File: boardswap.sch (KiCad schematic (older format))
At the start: 154 parts, among them J1 USB_C_Receptacle_USB2.0, SW1 SW_Push, U1 ATmega32U4-AU, Y1 16MHz

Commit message: did most placement
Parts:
- C7: footprint Diode_SMD:D_SOD-123 -> Capacitor_SMD:C_0805_2012Metric
- J1: footprint keyswitches:Kailh_socket_MX -> Connector_USB:USB_C_Receptacle_HRO_TYPE-C-31-M-12
- U1: footprint Package_QFP:TQFP-44_10x10mm_P0.8mm -> Package_DFN_QFN:QFN-44-1EP_7x7mm_P0.5mm_EP5.2x5.2mm
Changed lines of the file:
@@
 F 0 "J1" H 1307 7367 50  0000 C CNN
 F 1 "USB_C_Receptacle_USB2.0" H 1307 7276 50  0000 C CNN
-F 2 "keyswitches:Kailh_socket_MX" H 1350 6500 50  0001 C CNN
+F 2 "Connector_USB:USB_C_Receptacle_HRO_TYPE-C-31-M-12" H 1350 6500 50  0001 C CNN
 F 3 "https://www.usb.org/sites/default/files/documents/usb_type-c.zip" H 1350 6500 50  0001 C CNN
 	1    1200 6500
@@
 F 0 "C7" H 2042 3746 50  0000 L CNN
 F 1 "10uF" H 2042 3655 50  0000 L CNN
-F 2 "Diode_SMD:D_SOD-123" H 1950 3700 50  0001 C CNN
+F 2 "Capacitor_SMD:C_0805_2012Metric" H 1950 3700 50  0001 C CNN
 F 3 "~" H 1950 3700 50  0001 C CNN
 	1    1950 3700
@@
 F 0 "U1" H 3400 1111 50  0000 C CNN
 F 1 "ATmega32U4-AU" H 3400 1020 50  0000 C CNN
-F 2 "Package_QFP:TQFP-44_10x10mm_P0.8mm" H 3400 3000 50  0001 C CIN
+F 2 "Package_DFN_QFN:QFN-44-1EP_7x7mm_P0.5mm_EP5.2x5.2mm" H 3400 3000 50  0001 C CIN
 F 3 "http://ww1.microchip.com/downloads/en/DeviceDoc/Atmel-7766-8-bit-AVR-ATmega16U4-32U4_Datasheet.pdf" H 3400 3000 50  0001 C CNN
 	1    3400 3000

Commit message: hewwo backups owo
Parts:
- U1: footprint Package_DFN_QFN:QFN-44-1EP_7x7mm_P0.5mm_EP5.2x5.2mm -> Package_QFP:TQFP-44_10x10mm_P0.8mm
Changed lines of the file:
@@
 F 0 "U1" H 3400 1111 50  0000 C CNN
 F 1 "ATmega32U4-AU" H 3400 1020 50  0000 C CNN
-F 2 "Package_DFN_QFN:QFN-44-1EP_7x7mm_P0.5mm_EP5.2x5.2mm" H 3400 3000 50  0001 C CIN
+F 2 "Package_QFP:TQFP-44_10x10mm_P0.8mm" H 3400 3000 50  0001 C CIN
 F 3 "http://ww1.microchip.com/downloads/en/DeviceDoc/Atmel-7766-8-bit-AVR-ATmega16U4-32U4_Datasheet.pdf" H 3400 3000 50  0001 C CNN
 	1    3400 3000

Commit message: placed components
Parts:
- C4, C5, C6, C7: footprint Capacitor_SMD:C_0805_2012Metric -> Capacitor_SMD:C_0603_1608Metric
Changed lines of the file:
@@
 	1    0    0    -1
 $EndComp
-Connection ~ 2800 1500
 Wire Wire Line
 	2300 1500 2300 1200
@@
 	1    0    0    -1
 $EndComp
-Wire Wire Line
-	2800 1500 2800 1250
 $Comp
 L Device:R_Small R1
@@
 F 0 "C7" H 2042 3746 50  0000 L CNN
 F 1 "10uF" H 2042 3655 50  0000 L CNN
-F 2 "Capacitor_SMD:C_0805_2012Metric" H 1950 3700 50  0001 C CNN
+F 2 "Capacitor_SMD:C_0603_1608Metric" H 1950 3700 50  0001 C CNN
 F 3 "~" H 1950 3700 50  0001 C CNN
 	1    1950 3700
@@
 F 0 "C6" H 1642 3746 50  0000 L CNN
 F 1 "0.1uF" H 1642 3655 50  0000 L CNN
-F 2 "Capacitor_SMD:C_0805_2012Metric" H 1550 3700 50  0001 C CNN
+F 2 "Capacitor_SMD:C_0603_1608Metric" H 1550 3700 50  0001 C CNN
 F 3 "~" H 1550 3700 50  0001 C CNN
 	1    1550 3700
@@
 F 0 "C5" H 1242 3746 50  0000 L CNN
 F 1 "0.1uF" H 1242 3655 50  0000 L CNN
-F 2 "Capacitor_SMD:C_0805_2012Metric" H 1150 3700 50  0001 C CNN
+F 2 "Capacitor_SMD:C_0603_1608Metric" H 1150 3700 50  0001 C CNN
 F 3 "~" H 1150 3700 50  0001 C CNN
 	1    1150 3700
@@
 F 0 "C4" H 842 3746 50  0000 L CNN
 F 1 "0.1uF" H 842 3655 50  0000 L CNN
-F 2 "Capacitor_SMD:C_0805_2012Metric" H 750 3700 50  0001 C CNN
+F 2 "Capacitor_SMD:C_0603_1608Metric" H 750 3700 50  0001 C CNN
 F 3 "~" H 750 3700 50  0001 C CNN
 	1    750  3700
@@
 $EndComp
 Wire Wire Line
-	3300 4800 2950 4800
-Connection ~ 3300 4800
-Wire Wire Line
-	2950 4800 2950 4900
-Wire Wire Line
-	3400 4800 3300 4800
-$Comp
-L power:GND #PWR0109
-U 1 1 5F31D09C
-P 2950 4900
-F 0 "#PWR0109" H 2950 4650 50  0001 C CNN
-F 1 "GND" H 2955 4727 50  0000 C CNN
-F 2 "" H 2950 4900 50  0001 C CNN
-F 3 "" H 2950 4900 50  0001 C CNN
-	1    2950 4900
-	1    0    0    -1
-$EndComp
-Wire Wire Line
-	3400 1200 3400 1050
-Wire Wire Line
 	3400 1200 3500 1200
 Connection ~ 3400 1200
@@
 F 3 "" H 3400 1050 50  0001 C CNN
 	1    3400 1050
-	1    0    0    -1
-$EndComp
-$Comp
-L MCU_Microchip_ATmega:ATmega32U4-AU U1
-U 1 1 5F319131
-P 3400 3000
-F 0 "U1" H 3400 1111 50  0000 C CNN
-F 1 "ATmega32U4-AU" H 3400 1020 50  0000 C CNN
-F 2 "Package_QFP:TQFP-44_10x10mm_P0.8mm" H 3400 3000 50  0001 C CIN
-F 3 "http://ww1.microchip.com/downloads/en/DeviceDoc/Atmel-7766-8-bit-AVR-ATmega16U4-32U4_Datasheet.pdf" H 3400 3000 50  0001 C CNN
-	1    3400 3000
 	1    0    0    -1
 $EndComp
@@
 Text GLabel 10500 1200 1    50   Input ~ 0
 COL13
+Wire Wire Line
+	3400 1200 3400 1050
+Wire Wire Line
+	2800 1500 2800 1250
+$Comp
+L power:GND #PWR0109
+U 1 1 5F31D09C
+P 2950 4900
+F 0 "#PWR0109" H 2950 4650 50  0001 C CNN
+F 1 "GND" H 2955 4727 50  0000 C CNN
+F 2 "" H 2950 4900 50  0001 C CNN
+F 3 "" H 2950 4900 50  0001 C CNN
+	1    2950 4900
+	1    0    0    -1
+$EndComp
+Connection ~ 2800 1500
+Wire Wire Line
+	2950 4800 2950 4900
+$Comp
+L MCU_Microchip_ATmega:ATmega32U4-AU U1
+U 1 1 5F319131
+P 3400 3000
+F 0 "U1" H 3400 1111 50  0000 C CNN
+F 1 "ATmega32U4-AU" H 3400 1020 50  0000 C CNN
+F 2 "Package_QFP:TQFP-44_10x10mm_P0.8mm" H 3400 3000 50  0001 C CIN
+F 3 "http://ww1.microchip.com/downloads/en/DeviceDoc/Atmel-7766-8-bit-AVR-ATmega16U4-32U4_Datasheet.pdf" H 3400 3000 50  0001 C CNN
+	1    3400 3000
+	1    0    0    -1
+$EndComp
+Wire Wire Line
+	3400 4800 3300 4800
+Connection ~ 3300 4800
+Wire Wire Line
+	2950 4800 3300 4800
 $EndSCHEMATC

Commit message: done routing probably
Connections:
- net COL0: now also U1.11 (PB3)
- net COL10: now also U1.37 (PF6)
- net COL11: now also U1.36 (PF7)
- net COL12: now also U1.30 (PB6)
- net COL13: now also U1.28 (PB4)
- net COL2: now also U1.10 (PB2)
- net COL3: now also U1.9 (PB1)
- net COL4: now also U1.8 (PB0)
- net COL5: now also U1.1 (PE6)
- net COL6: now also U1.41 (PF0)
- net COL7: now also U1.40 (PF1)
- net COL8: now also U1.39 (PF4)
- net COL9: now also U1.38 (PF5)
- net ROW0: now also U1.19 (PD1)
- net ROW1: now also U1.20 (PD2)
- net ROW2: now also U1.21 (PD3)
- net ROW3: now also U1.22 (PD5)
- net ROW4: now also U1.18 (PD0)
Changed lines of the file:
@@
 Wire Wire Line
 	2950 4800 3300 4800
+Text GLabel 4000 3200 2    50   Input ~ 0
+ROW3
+Text GLabel 4000 3000 2    50   Input ~ 0
+ROW2
+Text GLabel 4000 2900 2    50   Input ~ 0
+ROW1
+Text GLabel 4000 2800 2    50   Input ~ 0
+ROW0
+Text GLabel 4000 2700 2    50   Input ~ 0
+ROW4
+Text GLabel 4000 1800 2    50   Input ~ 0
+COL0
+Text GLabel 4000 1700 2    50   Input ~ 0
+COL2
+Text GLabel 4000 1600 2    50   Input ~ 0
+COL3
+Text GLabel 4000 1500 2    50   Input ~ 0
+COL4
+Text GLabel 4000 3700 2    50   Input ~ 0
+COL5
+Text GLabel 4000 3900 2    50   Input ~ 0
+COL6
+Text GLabel 4000 4000 2    50   Input ~ 0
+COL7
+Text GLabel 4000 4100 2    50   Input ~ 0
+COL8
+Text GLabel 4000 4200 2    50   Input ~ 0
+COL9
+Text GLabel 4000 4300 2    50   Input ~ 0
+COL10
+Text GLabel 4000 4400 2    50   Input ~ 0
+COL11
+Text GLabel 4000 2100 2    50   Input ~ 0
+COL12
+Text GLabel 4000 1900 2    50   Input ~ 0
+COL13
 $EndSCHEMATC

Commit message: rotated mcu, begrudgingly
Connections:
- net COL0: now also U1.1 (PE6); no longer U1.11 (PB3)
- net COL10: now also U1.11 (PB3); no longer U1.37 (PF6)
- net COL11: now also U1.10 (PB2); no longer U1.36 (PF7)
- net COL12: now also U1.9 (PB1); no longer U1.30 (PB6)
- net COL13: now also U1.8 (PB0); no longer U1.28 (PB4)
- net COL2: now also U1.22 (PD5); no longer U1.10 (PB2)
- net COL3: now also U1.21 (PD3); no longer U1.9 (PB1)
- net COL4: now also U1.20 (PD2); no longer U1.8 (PB0)
- net COL5: now also U1.19 (PD1); no longer U1.1 (PE6)
- net COL6: now also U1.18 (PD0); no longer U1.41 (PF0)
- net COL7: now also U1.26 (PD6); no longer U1.40 (PF1)
- net COL8: now also U1.25 (PD4); no longer U1.39 (PF4)
- net COL9: now also U1.12 (PB7); no longer U1.38 (PF5)
- net ROW0: now also U1.38 (PF5); no longer U1.19 (PD1)
- net ROW1: now also U1.39 (PF4); no longer U1.20 (PD2)
- net ROW2: now also U1.40 (PF1); no longer U1.21 (PD3)
- net ROW3: now also U1.41 (PF0); no longer U1.22 (PD5)
- net ROW4: now also U1.37 (PF6); no longer U1.18 (PD0)
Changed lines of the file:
@@
 Wire Wire Line
 	2800 2800 2450 2800
-$Comp
-L Device:C_Small C3
-U 1 1 5F32256C
-P 2450 3000
-F 0 "C3" H 2542 3046 50  0000 L CNN
-F 1 "1uF" H 2542 2955 50  0000 L CNN
-F 2 "Capacitor_SMD:C_0805_2012Metric" H 2450 3000 50  0001 C CNN
-F 3 "~" H 2450 3000 50  0001 C CNN
-	1    2450 3000
-	1    0    0    -1
-$EndComp
 Wire Wire Line
 	1550 2600 1400 2600
@@
 Wire Wire Line
 	2950 4800 3300 4800
+Text GLabel 4000 3900 2    50   Input ~ 0
+ROW3
+Text GLabel 4000 4000 2    50   Input ~ 0
+ROW2
+Text GLabel 4000 4100 2    50   Input ~ 0
+ROW1
+Text GLabel 4000 4200 2    50   Input ~ 0
+ROW0
+Text GLabel 4000 4300 2    50   Input ~ 0
+ROW4
+Text GLabel 4000 3700 2    50   Input ~ 0
+COL0
+Text GLabel 4000 3000 2    50   Input ~ 0
+COL3
+Text GLabel 4000 2900 2    50   Input ~ 0
+COL4
+Text GLabel 4000 2800 2    50   Input ~ 0
+COL5
+Text GLabel 4000 2700 2    50   Input ~ 0
+COL6
+Text GLabel 4000 3300 2    50   Input ~ 0
+COL7
+Text GLabel 4000 3100 2    50   Input ~ 0
+COL8
+Text GLabel 4000 2200 2    50   Input ~ 0
+COL9
+Text GLabel 4000 1800 2    50   Input ~ 0
+COL10
+Text GLabel 4000 1700 2    50   Input ~ 0
+COL11
+Text GLabel 4000 1600 2    50   Input ~ 0
+COL12
+Text GLabel 4000 1500 2    50   Input ~ 0
+COL13
+$Comp
+L Device:C_Small C3
+U 1 1 5F32256C
+P 2450 3000
+F 0 "C3" H 2542 3046 50  0000 L CNN
+F 1 "1uF" H 2542 2955 50  0000 L CNN
+F 2 "Capacitor_SMD:C_0805_2012Metric" H 2450 3000 50  0001 C CNN
+F 3 "~" H 2450 3000 50  0001 C CNN
+	1    2450 3000
+	1    0    0    -1
+$EndComp
 Text GLabel 4000 3200 2    50   Input ~ 0
-ROW3
-Text GLabel 4000 3000 2    50   Input ~ 0
-ROW2
-Text GLabel 4000 2900 2    50   Input ~ 0
-ROW1
-Text GLabel 4000 2800 2    50   Input ~ 0
-ROW0
-Text GLabel 4000 2700 2    50   Input ~ 0
-ROW4
-Text GLabel 4000 1800 2    50   Input ~ 0
-COL0
-Text GLabel 4000 1700 2    50   Input ~ 0
 COL2
-Text GLabel 4000 1600 2    50   Input ~ 0
-COL3
-Text GLabel 4000 1500 2    50   Input ~ 0
-COL4
-Text GLabel 4000 3700 2    50   Input ~ 0
-COL5
-Text GLabel 4000 3900 2    50   Input ~ 0
-COL6
-Text GLabel 4000 4000 2    50   Input ~ 0
-COL7
-Text GLabel 4000 4100 2    50   Input ~ 0
-COL8
-Text GLabel 4000 4200 2    50   Input ~ 0
-COL9
-Text GLabel 4000 4300 2    50   Input ~ 0
-COL10
-Text GLabel 4000 4400 2    50   Input ~ 0
-COL11
-Text GLabel 4000 2100 2    50   Input ~ 0
-COL12
-Text GLabel 4000 1900 2    50   Input ~ 0
-COL13
 $EndSCHEMATC

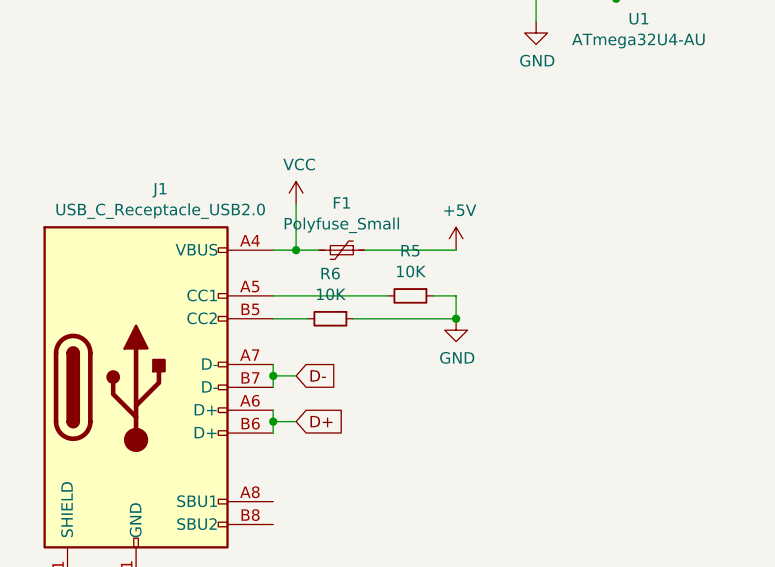
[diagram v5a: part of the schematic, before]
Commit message: fixed resistor values
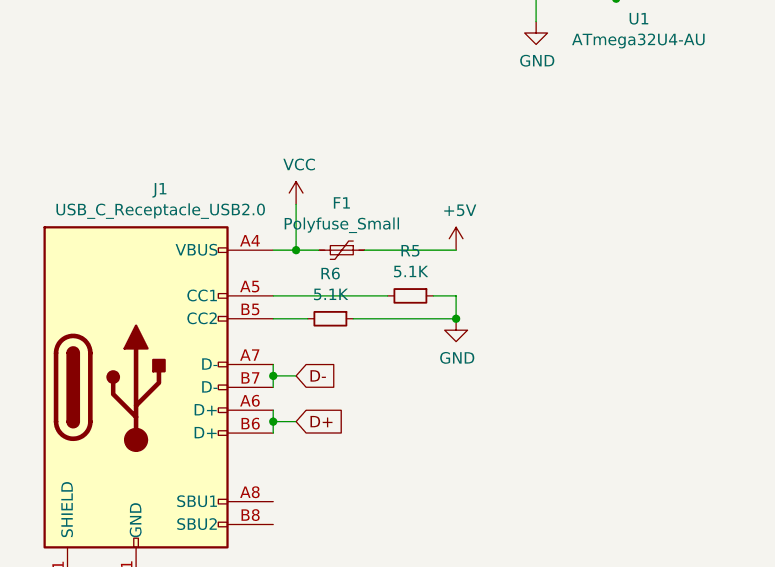
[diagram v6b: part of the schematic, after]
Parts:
- R5, R6: value 10K -> 5.1K
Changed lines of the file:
@@
 P 2050 6200
 F 0 "R6" V 1854 6200 50  0000 C CNN
-F 1 "10K" V 1945 6200 50  0000 C CNN
+F 1 "5.1K" V 1945 6200 50  0000 C CNN
 F 2 "Resistor_SMD:R_0805_2012Metric" H 2050 6200 50  0001 C CNN
 F 3 "~" H 2050 6200 50  0001 C CNN
@@
 P 2400 6100
 F 0 "R5" V 2204 6100 50  0000 C CNN
-F 1 "10K" V 2295 6100 50  0000 C CNN
+F 1 "5.1K" V 2295 6100 50  0000 C CNN
 F 2 "Resistor_SMD:R_0805_2012Metric" H 2400 6100 50  0001 C CNN
 F 3 "~" H 2400 6100 50  0001 C CNN

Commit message: fixed silkscreen
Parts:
- MX1, MX10, MX11, MX12, MX13, MX14, MX15, MX16, MX17, MX18, MX19, MX2, MX20, MX21, MX22, MX23, MX24, MX25, MX26, MX27, MX28, MX29, MX3, MX30, MX31, MX32, MX33, MX34, MX35, MX36, MX37, MX38, MX39, MX4, MX40, MX41, MX42, MX43, MX44, MX45, MX46, MX47, MX48, MX49, MX5, MX50, MX51, MX52, MX53, MX54, MX55, MX56, MX57, MX58, MX59, MX6, MX60, MX61, MX62, MX63, MX64, MX65, MX66, MX67, MX68, MX7, MX8, MX9: footprint keyswitches:Kailh_socket_MX -> keyswitches:Kailh_socket_MX_alt

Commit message: removed unnecessary files
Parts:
- MX1, MX10, MX11, MX12, MX13, MX14, MX15, MX16, MX17, MX18, MX19, MX2, MX20, MX21, MX22, MX23, MX24, MX25, MX26, MX27, MX28, MX29, MX3, MX30, MX31, MX32, MX33, MX34, MX35, MX36, MX37, MX38, MX39, MX4, MX40, MX41, MX42, MX43, MX44, MX45, MX46, MX47, MX48, MX49, MX5, MX50, MX51, MX52, MX53, MX54, MX55, MX56, MX57, MX58, MX59, MX6, MX60, MX61, MX62, MX63, MX64, MX65, MX66, MX67, MX68, MX7, MX8, MX9: footprint keyswitches:Kailh_socket_MX_alt -> switchprint:Kailh_socket_MX_alt
